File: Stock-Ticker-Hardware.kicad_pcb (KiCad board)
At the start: 2 copper layers, 60 x 50 mm, 16 parts, among them J1 Conn_01x05_Socket, J2 Conn_01x03_Pin, J3 Conn_01x03_Socket, SW1 SW_Push, U1 74AHCT125

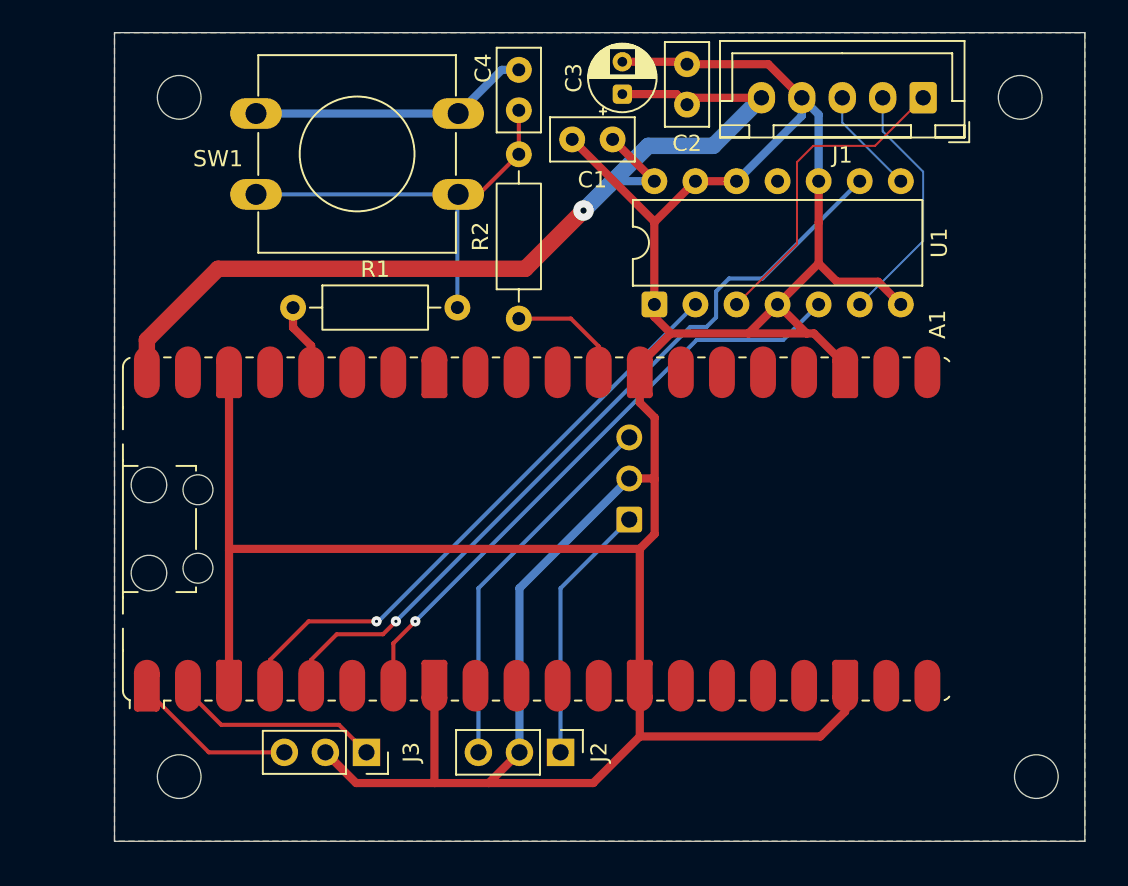
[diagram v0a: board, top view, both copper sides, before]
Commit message: Add silk text pin labels
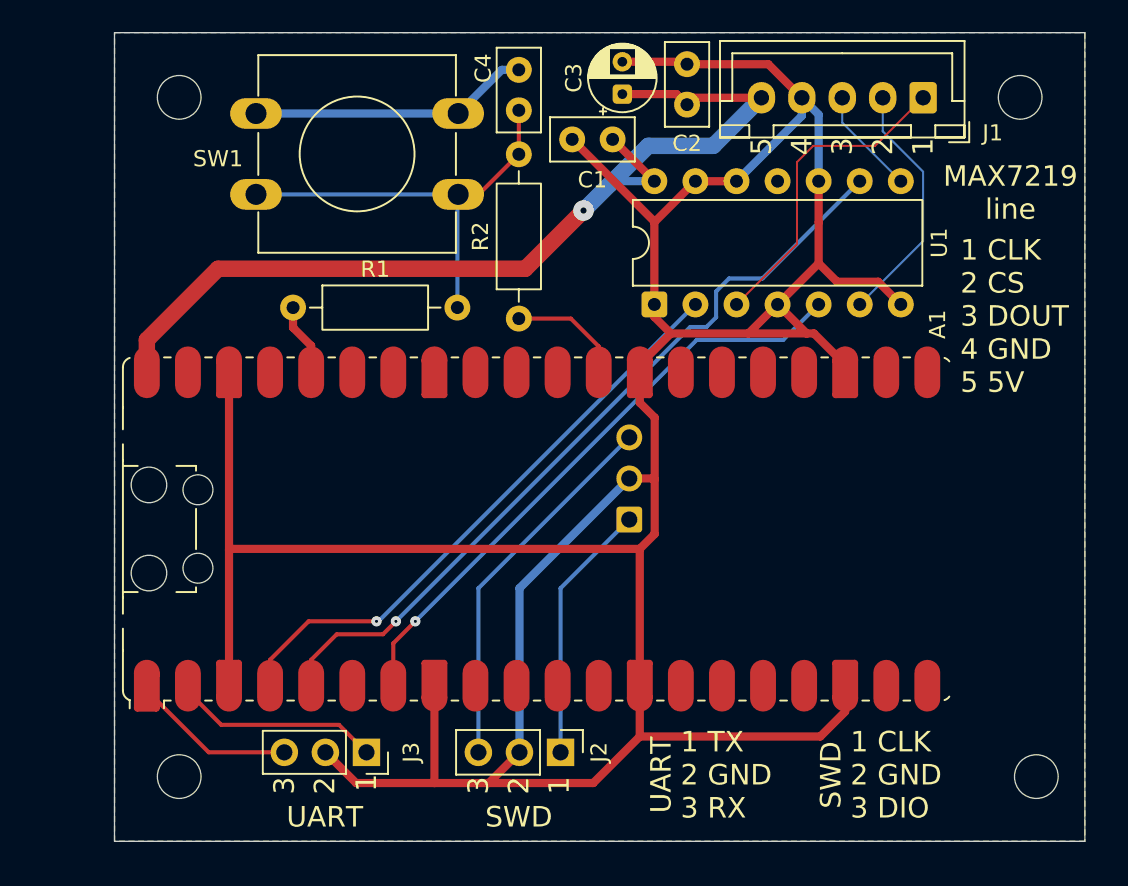
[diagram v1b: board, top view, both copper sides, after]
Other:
- board text added: "1"
- board text added: "1 CLK 2 CS 3 DOUT 4 GND 5 5V"
- board text added: "1 CLK 2 GND 3 DIO"
- board text added: "1 TX 2 GND 3 RX"
- board text added: "2"
- board text added: "3"
- board text added: "4"
- board text added: "5"
- board text added: "MAX7219 line"
- board text added: "SWD"
- board text added: "UART"
- board text added: "https://github.com/ UnsignedArduino/ Stock-Ticker-Hardware Rev ${VERSION}"
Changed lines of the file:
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@@
 	(title_block
 		(title "Stock Ticker Hardware")
-		(rev "1")
+		(rev "${VERSION}")
 	)
 	(layers
@@
 		)
 	)
+	(property "VERSION" "1")
 	(net 0 "")
 	(net 1 "unconnected-(A1-3V3_EN-Pad37)")
@@
 		(tags "connector JST XH vertical")
 		(property "Reference" "J1"
-			(at 5 -3.55 0)
+			(at -4.3 -2.175 0)
 			(layer "F.SilkS")
 			(effects
@@
 		(layer "Edge.Cuts")
 	)
+	(gr_text "SWD"
+		(at 75 98.5 0)
+		(layer "F.SilkS")
+		(effects
+			(font
+				(size 1.27 1.27)
+				(thickness 0.2)
+			)
+		)
+	)
+	(gr_text "2"
+		(at 63 96 90)
+		(layer "F.SilkS")
+		(effects
+			(font
+				(size 1.27 1.27)
+				(thickness 0.2)
+			)
+			(justify right)
+		)
+	)
+	(gr_text "UART"
+		(at 83.8 95.9 90)
+		(layer "F.SilkS")
+		(effects
+			(font
+				(size 1.27 1.27)
+				(thickness 0.2)
+			)
+		)
+	)
+	(gr_text "4"
+		(at 92.5 56.485 90)
+		(layer "F.SilkS")
+		(effects
+			(font
+				(size 1.27 1.27)
+				(thickness 0.2)
+			)
+			(justify right)
+		)
+	)
+	(gr_text "1"
+		(at 77.5 96 90)
+		(layer "F.SilkS")
+		(effects
+			(font
+				(size 1.27 1.27)
+				(thickness 0.2)
+			)
+			(justify right)
+		)
+	)
+	(gr_text "3"
+		(at 72.5 96 90)
+		(layer "F.SilkS")
+		(effects
+			(font
+				(size 1.27 1.27)
+				(thickness 0.2)
+			)
+			(justify right)
+		)
+	)
+	(gr_text "3"
+		(at 95 56.475 90)
+		(layer "F.SilkS")
+		(effects
+			(font
+				(size 1.27 1.27)
+				(thickness 0.2)
+			)
+			(justify right)
+		)
+	)
+	(gr_text "2"
+		(at 97.5 56.475 90)
+		(layer "F.SilkS")
+		(effects
+			(font
+				(size 1.27 1.27)
+				(thickness 0.2)
+			)
+			(justify right)
+		)
+	)
+	(gr_text "UART"
+		(at 63 98.5 0)
+		(layer "F.SilkS")
+		(effects
+			(font
+				(size 1.27 1.27)
+				(thickness 0.2)
+			)
+		)
+	)
+	(gr_text "SWD"
+		(at 94.3 95.9 90)
+		(layer "F.SilkS")
+		(effects
+			(font
+				(size 1.27 1.27)
+				(thickness 0.2)
+			)
+		)
+	)
+	(gr_text "1 TX\n2 GND\n3 RX"
+		(at 85 95.9 0)
+		(layer "F.SilkS")
+		(effects
+			(font
+				(size 1.27 1.27)
+				(thickness 0.2)
+			)
+			(justify left)
+		)
+	)
+	(gr_text "5"
+		(at 90 56.475 90)
+		(layer "F.SilkS")
+		(effects
+			(font
+				(size 1.27 1.27)
+				(thickness 0.2)
+			)
+			(justify right)
+		)
+	)
+	(gr_text "MAX7219\nline"
+		(at 105.4 59.9 0)
+		(layer "F.SilkS")
+		(effects
+			(font
+				(size 1.27 1.27)
+				(thickness 0.2)
+			)
+		)
+	)
+	(gr_text "1 CLK\n2 GND\n3 DIO"
+		(at 95.5 95.9 0)
+		(layer "F.SilkS")
+		(effects
+			(font
+				(size 1.27 1.27)
+				(thickness 0.2)
+			)
+			(justify left)
+		)
+	)
+	(gr_text "1"
+		(at 65.58 95.83 90)
+		(layer "F.SilkS")
+		(effects
+			(font
+				(size 1.27 1.27)
+				(thickness 0.2)
+			)
+			(justify right)
+		)
+	)
+	(gr_text "3"
+		(at 60.5 96 90)
+		(layer "F.SilkS")
+		(effects
+			(font
+				(size 1.27 1.27)
+				(thickness 0.2)
+			)
+			(justify right)
+		)
+	)
+	(gr_text "1"
+		(at 100 56.5 90)
+		(layer "F.SilkS")
+		(effects
+			(font
+				(size 1.27 1.27)
+				(thickness 0.2)
+			)
+			(justify right)
+		)
+	)
+	(gr_text "2"
+		(at 75 96 90)
+		(layer "F.SilkS")
+		(effects
+			(font
+				(size 1.27 1.27)
+				(thickness 0.2)
+			)
+			(justify right)
+		)
+	)
+	(gr_text "1 CLK\n2 CS\n3 DOUT\n4 GND\n5 5V"
+		(at 102.3 62.7 0)
+		(layer "F.SilkS")
+		(effects
+			(font
+				(size 1.27 1.27)
+				(thickness 0.2)
+			)
+			(justify left top)
+		)
+	)
+	(gr_text "https://github.com/\nUnsignedArduino/\nStock-Ticker-Hardware\n\nRev ${VERSION}"
+		(at 109 81 0)
+		(layer "B.SilkS")
+		(effects
+			(font
+				(size 1.27 1.27)
+				(thickness 0.2)
+			)
+			(justify left mirror)
+		)
+	)
 	(segment

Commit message: Points for power rails and ground
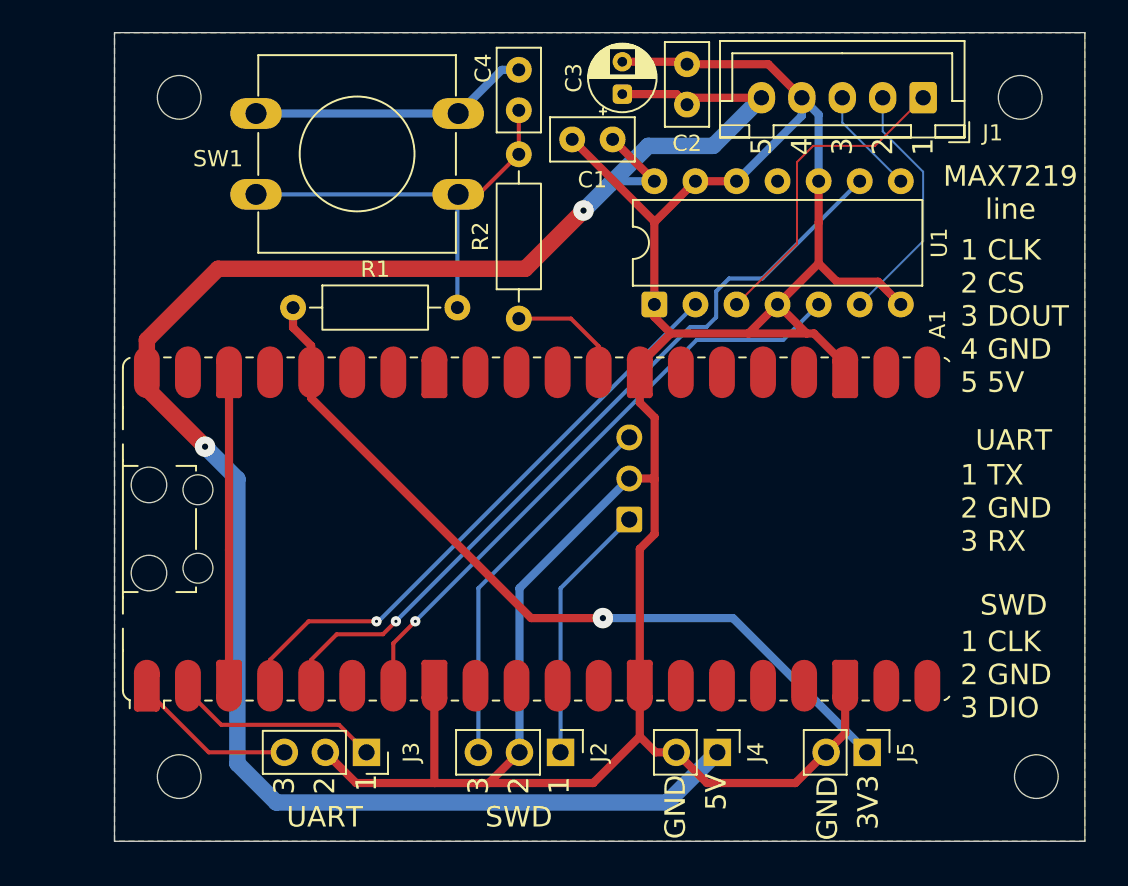
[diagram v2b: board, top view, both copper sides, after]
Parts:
- added J4: Conn_01x02_Pin, Connector_PinHeader_2.54mm:PinHeader_1x02_P2.54mm_Vertical, F.Cu at (87.3, 94.5)
- added J5: Conn_01x02_Pin, Connector_PinHeader_2.54mm:PinHeader_1x02_P2.54mm_Vertical, F.Cu at (96.5, 94.5)
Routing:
- net +5V: track 62.7 -> 121.2 mm, vias 1 -> 2
- net +3.3V: track 4.46 -> 49.5 mm, vias 0 -> 1
- net GND: track 233.0 -> 210.8 mm
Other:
- board text added: "3V3"
- board text added: "5V"
- board text added: "GND"

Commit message: Shift pin headers up for silk text space
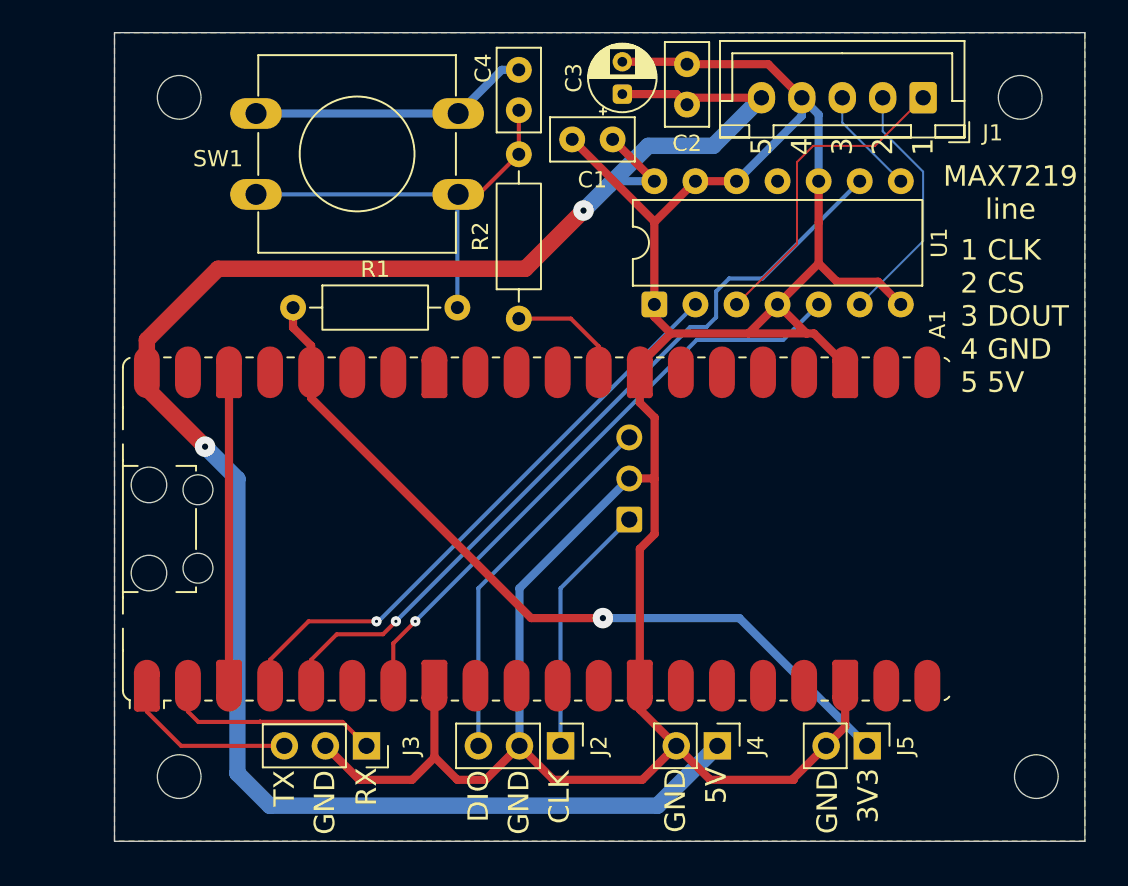
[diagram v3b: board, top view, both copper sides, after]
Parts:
- moved J2 0.40 mm to (77.6, 94.1)
- moved J3 0.40 mm to (65.6, 94.1)
- moved J4 0.40 mm to (87.3, 94.1)
- moved J5 0.40 mm to (96.5, 94.1)
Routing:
- net GND: track 210.8 -> 209.7 mm
- net +5V: track 121.2 -> 121.8 mm
- net /UART0_TX: track 10.4 -> 11.0 mm
- net /UART0_RX: track 13.0 -> 13.5 mm
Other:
- board text added: "CLK"
- board text added: "DIO"
- board text added: "RX"
- board text added: "TX"
- board text removed: "1 CLK 2 GND 3 DIO"
- board text removed: "1 TX 2 GND 3 RX"
- board text removed: "SWD"
- board text removed: "UART"

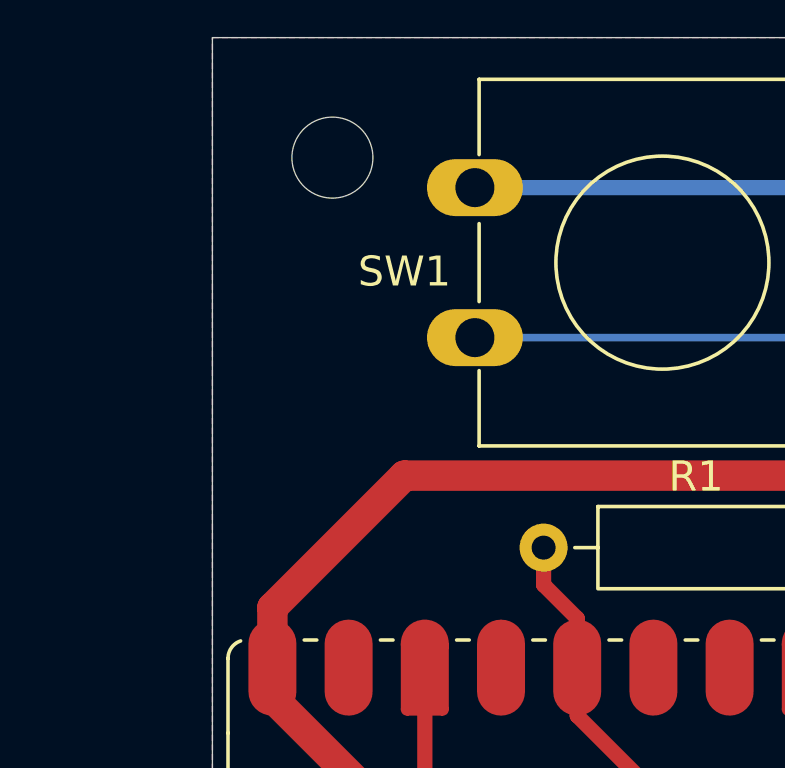
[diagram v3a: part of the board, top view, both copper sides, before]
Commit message: Move info silk around
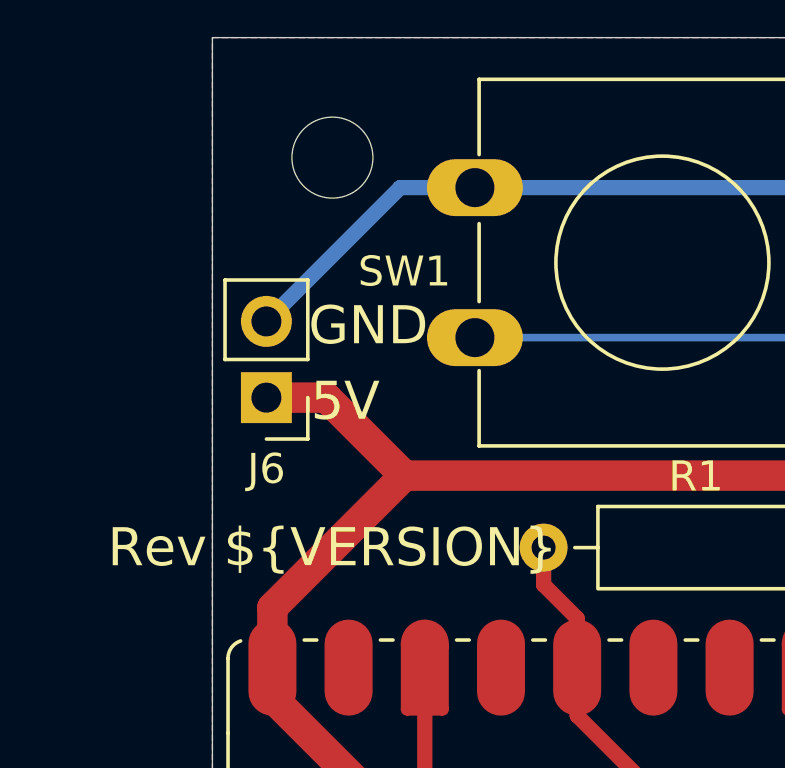
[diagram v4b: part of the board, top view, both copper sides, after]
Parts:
- added J6: Conn_01x02_Pin, Connector_PinHeader_2.54mm:PinHeader_1x02_P2.54mm_Vertical, F.Cu at (51.8, 62.0)
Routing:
- net GND: track 209.7 -> 218.5 mm
- net +5V: track 121.8 -> 127.5 mm
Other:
- board text added: "Rev ${VERSION}"
- board text added: "https://github.com/ UnsignedArduino/ Stock-Ticker-Hardware"
- board text removed: "https://github.com/ UnsignedArduino/ Stock-Ticker-Hardware Rev ${VERSION}"

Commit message: Cleanup tracks
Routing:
- net GND: track 218.5 -> 216.4 mm
- net +5V: track 127.5 -> 125.6 mm
- net Net-(C4-Pad1): track 27.1 -> 25.7 mm
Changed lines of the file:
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@@
-	)
-	(segment
-		(start 85.25 51.8)
-		(end 85.4 51.95)
-		(width 0.508)
-		(layer "F.Cu")
-		(net 14)
-	)
-	(segment
-		(start 57.08 70.529584)
-		(end 57.08 71)
-		(width 0.508)
-		(layer "F.Cu")
-		(net 14)
 	)
 	(segment
@@
 	)
 	(segment
-		(start 93.54 61.725)
+		(start 93.54 59.185)
 		(end 93.54 64.265)
 		(width 0.508)
@@
 	)
 	(segment
-		(start 93.54 59.185)
-		(end 93.54 61.725)
-		(width 0.508)
-		(layer "F.Cu")
-		(net 14)
-	)
-	(segment
-		(start 71.25 55)
-		(end 71.7 55)
-		(width 0.508)
-		(layer "F.Cu")
-		(net 14)
-	)
-	(segment
 		(start 84.4 68.6)
 		(end 82.48 70.52)
@@
 	)
 	(segment
-		(start 91 66.805)
-		(end 91.005 66.805)
-		(width 0.508)
-		(layer "F.Cu")
-		(net 14)
-	)
-	(segment
-		(start 57.08 82)
-		(end 57.08 71)
-		(width 0.508)
-		(layer "F.Cu")
-		(net 14)
-	)
-	(segment
 		(start 94 94.1)
 		(end 95.18 92.92)
@@
 	(segment
 		(start 57.08 90.38)
-		(end 57.08 82)
+		(end 57.08 71)
 		(width 0.508)
 		(layer "F.Cu")
@@
 	)
 	(segment
-		(start 91 66.805)
-		(end 90.995 66.805)
-		(width 0.508)
-		(layer "F.Cu")
-		(net 14)
-	)
-	(segment
-		(start 82.48 70.52)
-		(end 82.48 71)
-		(width 0.508)
-		(layer "F.Cu")
-		(net 14)
-	)
-	(segment
 		(start 71.2 96.2)
 		(end 72.94 96.2)
@@
 		(start 81.4 51.8)
 		(end 85.25 51.8)
-		(width 0.508)
-		(layer "F.Cu")
-		(net 14)
-	)
-	(segment
-		(start 95.18 71)
-		(end 95.18 70.529584)
 		(width 0.508)
 		(layer "F.Cu")
@@
 	)
 	(segment
-		(start 89.575 54.45)
-		(end 90 54.025)
-		(width 0.508)
-		(layer "F.Cu")
-		(net 32)
-	)
-	(segment
 		(start 84.75 53.8)
 		(end 85.4 54.45)
@@
 	)
 	(segment
-		(start 52 71)
-		(end 52 72)
-		(width 1.016)
-		(layer "F.Cu")
-		(net 32)
-	)
-	(segment
 		(start 53.8 62)
 		(end 51.8 62)
@@
 	)
 	(segment
-		(start 83.38 59.185)
-		(end 83.38 59.18)
-		(width 0.508)
-		(layer "F.Cu")
-		(net 32)
-	)
-	(segment
 		(start 90 54.025)
 		(end 85.825 54.025)
-		(width 0.508)
-		(layer "F.Cu")
-		(net 32)
-	)
-	(segment
-		(start 83.38 59.185)
-		(end 83.065 59.185)
 		(width 0.508)
 		(layer "F.Cu")
@@
 	)
 	(segment
-		(start 71.25 66.95)
-		(end 71.2 67)
-		(width 0.254)
-		(layer "F.Cu")
-		(net 41)
-	)
-	(segment
-		(start 71.25 60)
-		(end 72.52 60)
-		(width 0.254)
-		(layer "F.Cu")
-		(net 41)
-	)
-	(segment
 		(start 75 54.8)
 		(end 75 57.52)
@@
 		(width 0.254)
 		(layer "B.Cu")
-		(net 41)
-	)
-	(segment
-		(start 71.2 60.05)
-		(end 71.25 60)
-		(width 0.254)
-		(layer "B.Cu")
